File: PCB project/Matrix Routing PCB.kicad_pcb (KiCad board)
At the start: 4 copper layers, 87 x 35 mm, 14 parts, among them J1 53261-0471, J2 JST_PH_S4B-PH-SM4-TB, J3 ESQ-105-23-T-D, J4 TSM-102-01-L-DH-A, J5 USB-A-S-F-B-SM2-R-TR, U1 FT232RL

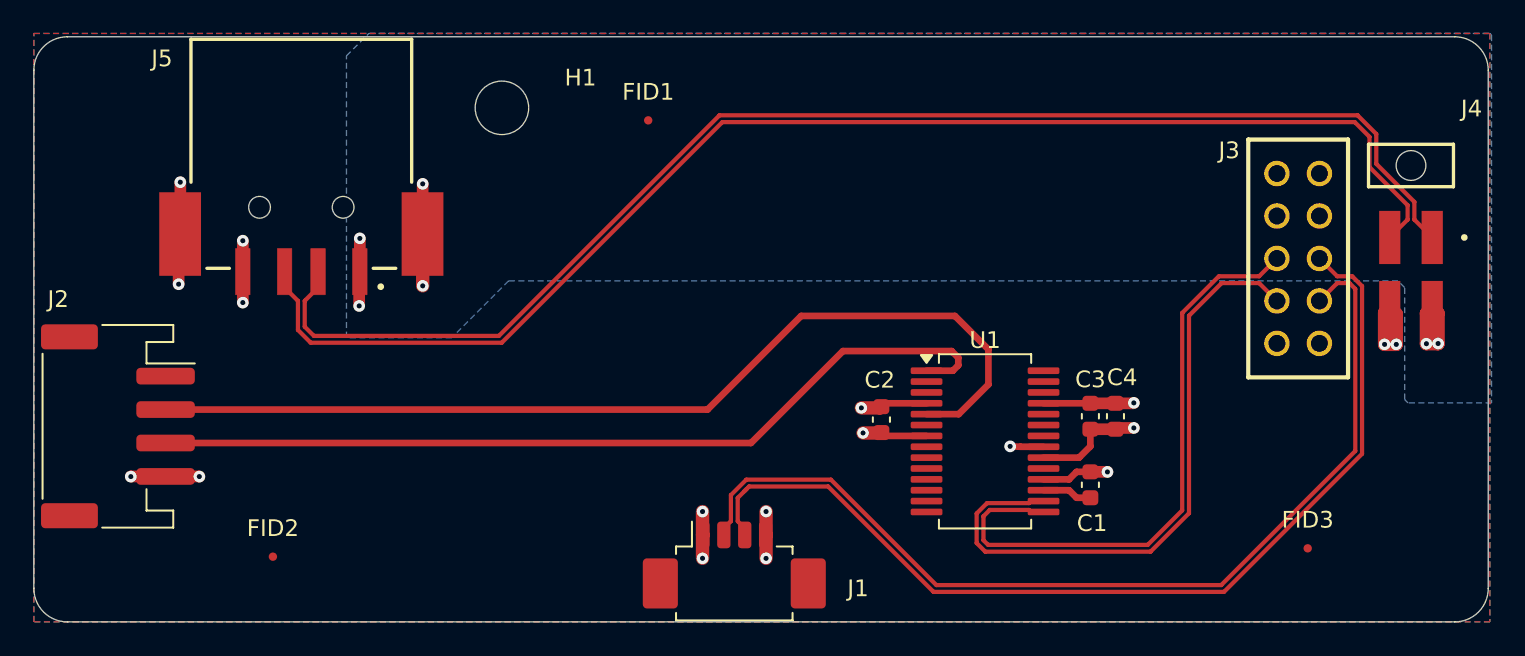
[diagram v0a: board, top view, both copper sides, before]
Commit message: Move J2 2.41mm forward
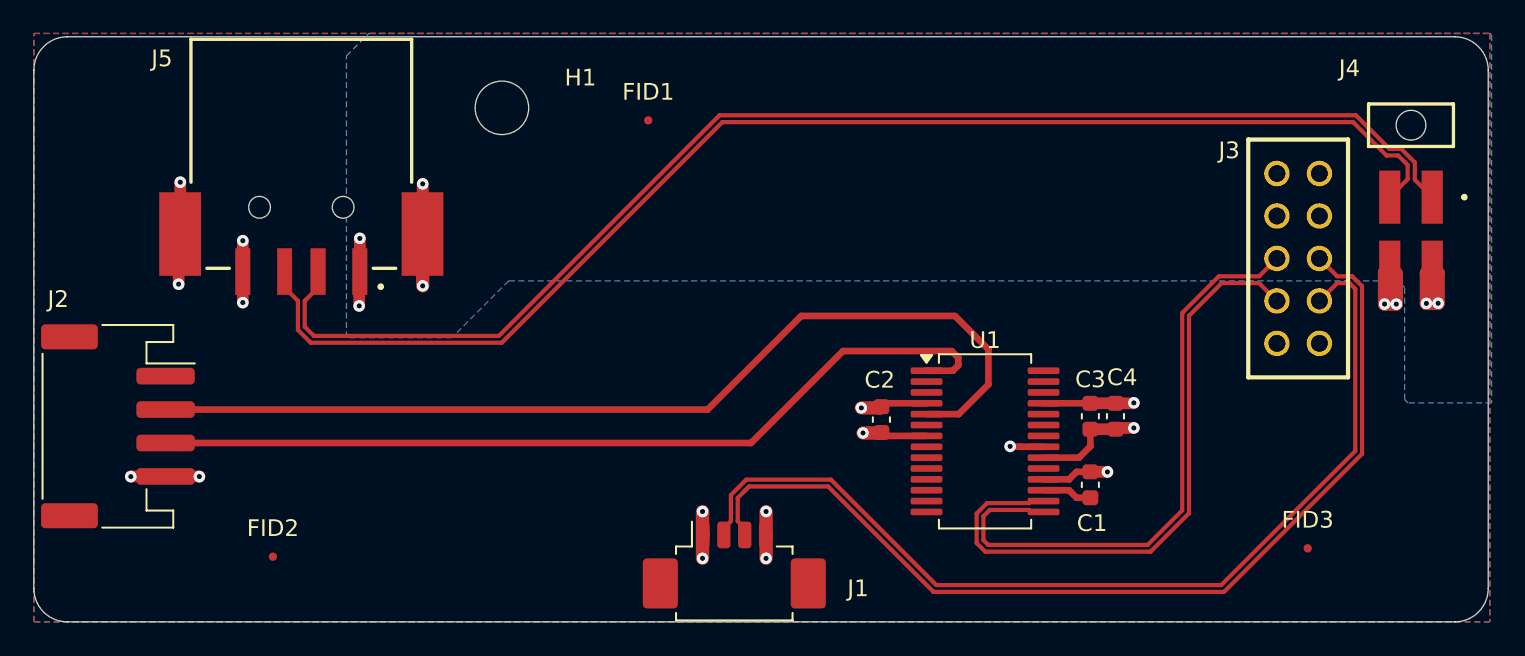
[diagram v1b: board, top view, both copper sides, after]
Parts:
- moved J4 2.41 mm to (257.3, 76.9)
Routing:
- net /USB_OTG_DN: track 81.5 -> 79.4 mm
- net /USB_OTG_DP: track 81.5 -> 79.4 mm
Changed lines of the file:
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@@
 	(footprint "Matrix Routing PCB:SAMTEC_TSM-102-01-L-DH-A"
 		(layer "F.Cu")
-		(at 257.279151 79.275)
+		(at 257.279151 76.865)
 		(property "Reference" "J4"
-			(at 3.620849 -3.4 0)
+			(at -3.679151 -3.4 0)
 			(layer "F.SilkS")
 			(effects
@@
 		(layer "Dwgs.User")
 		(pts
-			(xy 257.279151 78.005) (xy 257.279151 71.575)
-		)
-		(height 0)
-		(orientation 1)
-		(format
-			(prefix "")
-			(suffix "")
-			(units 3)
-			(units_format 0)
-			(precision 4)
-			(suppress_zeroes yes)
-		)
-		(style
-			(thickness 0.1)
-			(arrow_length 1.27)
-			(text_position_mode 0)
-			(arrow_direction outward)
-			(extension_height 0.58642)
-			(extension_offset 0.5)
-			(keep_text_aligned yes)
-		)
-		(gr_text "6.43"
-			(at 256.129151 74.79 90)
-			(layer "Dwgs.User")
-			(effects
-				(font
-					(size 1 1)
-					(thickness 0.15)
-				)
-			)
-		)
-	)
-	(dimension
-		(type orthogonal)
-		(layer "Dwgs.User")
-		(pts
 			(xy 248.054 78.231) (xy 248.054 71.575)
 		)
@@
 		(layer "Dwgs.User")
 		(pts
-			(xy 257.03 92.26) (xy 257.03 106.575)
-		)
-		(height 0)
-		(orientation 1)
-		(format
-			(prefix "")
-			(suffix "")
-			(units 3)
-			(units_format 0)
-			(precision 4)
-			(suppress_zeroes yes)
-		)
-		(style
-			(thickness 0.1)
-			(arrow_length 1.27)
-			(text_position_mode 0)
-			(arrow_direction outward)
-			(extension_height 0.58642)
-			(extension_offset 0.5)
-			(keep_text_aligned yes)
-		)
-		(gr_text "14.315"
-			(at 255.88 99.4175 90)
-			(layer "Dwgs.User")
-			(effects
-				(font
-					(size 1 1)
-					(thickness 0.15)
-				)
-			)
-		)
-	)
-	(dimension
-		(type orthogonal)
-		(layer "Dwgs.User")
-		(pts
 			(xy 174.9 106.575) (xy 261.9 106.575)
 		)
@@
 	)
 	(segment
-		(start 255.7 88.079151)
-		(end 256.009151 87.77)
+		(start 255.7 85.669151)
+		(end 256.009151 85.36)
 		(width 0.8)
 		(layer "F.Cu")
@@
 	)
 	(segment
-		(start 256.4 88.160849)
-		(end 256.009151 87.77)
+		(start 256.4 85.750849)
+		(end 256.009151 85.36)
 		(width 0.8)
 		(layer "F.Cu")
@@
 	)
 	(segment
-		(start 255.7 89.975)
-		(end 255.7 88.079151)
+		(start 255.7 87.565)
+		(end 255.7 85.669151)
 		(width 0.8)
 		(layer "F.Cu")
@@
 	)
 	(segment
-		(start 256.4 89.975)
-		(end 256.4 88.160849)
+		(start 256.4 87.565)
+		(end 256.4 85.750849)
 		(width 0.8)
 		(layer "F.Cu")
@@
 	)
 	(segment
-		(start 255.7 89.975)
-		(end 256.4 89.975)
+		(start 255.7 87.565)
+		(end 256.4 87.565)
 		(width 0.8)
 		(layer "F.Cu")
@@
 	)
 	(via
-		(at 256.4 89.975)
+		(at 256.4 87.565)
 		(size 0.7)
 		(drill 0.3)
@@
 	)
 	(via
-		(at 255.7 89.975)
+		(at 255.7 87.565)
 		(size 0.7)
 		(drill 0.3)
@@
 	)
 	(segment
-		(start 191.103 87.372)
-		(end 191.9 86.575)
+		(start 257.508 80.128849)
+		(end 257.508 79.095914)
 		(width 0.254)
 		(layer "F.Cu")
@@
 	)
 	(segment
-		(start 258.549151 83.58)
-		(end 257.482151 82.513)
+		(start 256.684086 78.272)
+		(end 255.984086 78.272)
 		(width 0.254)
 		(layer "F.Cu")
@@
 	)
 	(segment
-		(start 215.915914 76.272)
-		(end 202.718916 89.469)
+		(start 202.718916 89.469)
+		(end 191.654425 89.469)
 		(width 0.254)
 		(layer "F.Cu")
@@
 	)
 	(segment
-		(start 257.482151 82.513)
-		(end 257.482151 81.454151)
+		(start 215.915914 76.272)
+		(end 202.718916 89.469)
 		(width 0.254)
 		(layer "F.Cu")
@@
 	)
 	(segment
-		(start 255.203 77.390914)
-		(end 254.084084 76.272)
+		(start 258.549151 81.17)
+		(end 257.508 80.128849)
 		(width 0.254)
 		(layer "F.Cu")
@@
 	)
 	(segment
-		(start 191.9 86.575)
-		(end 191.9 85.625)
+		(start 257.508 79.095914)
+		(end 256.684086 78.272)
 		(width 0.254)
 		(layer "F.Cu")
@@
 	)
 	(segment
-		(start 255.203 77.390914)
-		(end 255.203 79.175)
+		(start 191.103 88.917575)
+		(end 191.103 87.372)
 		(width 0.254)
 		(layer "F.Cu")
@@
 	)
 	(segment
-		(start 191.103 88.917575)
-		(end 191.103 87.372)
+		(start 255.984086 78.272)
+		(end 253.984086 76.272)
 		(width 0.254)
 		(layer "F.Cu")
@@
 	)
 	(segment
-		(start 257.482151 81.454151)
-		(end 255.203 79.175)
+		(start 191.654425 89.469)
+		(end 191.103 88.917575)
 		(width 0.254)
 		(layer "F.Cu")
@@
 	)
 	(segment
-		(start 254.084084 76.272)
-		(end 215.915914 76.272)
+		(start 191.9 86.575)
+		(end 191.9 85.625)
 		(width 0.254)
 		(layer "F.Cu")
@@
 	)
 	(segment
-		(start 191.654425 89.469)
-		(end 202.718916 89.469)
+		(start 253.984086 76.272)
+		(end 215.915914 76.272)
 		(width 0.254)
 		(layer "F.Cu")
@@
 	)
 	(segment
-		(start 191.654425 89.469)
-		(end 191.103 88.917575)
+		(start 191.103 87.372)
+		(end 191.9 86.575)
 		(width 0.254)
 		(layer "F.Cu")
@@
 	)
 	(segment
-		(start 258.2 88.119151)
-		(end 258.549151 87.77)
+		(start 258.2 85.709151)
+		(end 258.549151 85.36)
 		(width 0.8)
 		(layer "F.Cu")
@@
 	)
 	(segment
-		(start 258.2 89.935)
-		(end 258.2 88.119151)
+		(start 258.2 87.525)
+		(end 258.2 85.709151)
 		(width 0.8)
 		(layer "F.Cu")
@@
 	)
 	(segment
-		(start 258.9 89.925)
-		(end 258.9 88.120849)
+		(start 258.9 87.515)
+		(end 258.9 85.710849)
 		(width 0.8)
 		(layer "F.Cu")
@@
 	)
 	(segment
-		(start 258.89 89.935)
-		(end 258.9 89.925)
+		(start 258.89 87.525)
+		(end 258.9 87.515)
 		(width 0.8)
 		(layer "F.Cu")
@@
 	)
 	(segment
-		(start 258.2 89.935)
-		(end 258.89 89.935)
+		(start 258.2 87.525)
+		(end 258.89 87.525)
 		(width 0.8)
 		(layer "F.Cu")
@@
 	)
 	(segment
-		(start 258.9 88.120849)
-		(end 258.549151 87.77)
+		(start 258.9 85.710849)
+		(end 258.549151 85.36)
 		(width 0.8)
 		(layer "F.Cu")
@@
 	)
 	(via
-		(at 258.2 89.935)
+		(at 258.2 87.525)
 		(size 0.7)
 		(drill 0.3)
@@
 	)
 	(via
-		(at 258.9 89.925)
+		(at 258.9 87.515)
 		(size 0.7)
 		(drill 0.3)
@@
 	)
 	(segment
-		(start 216.084914 76.68)
-		(end 253.915085 76.68)
+		(start 190.697 87.372)
+		(end 189.9 86.575)
 		(width 0.254)
 		(layer "F.Cu")
@@
 	)
 	(segment
-		(start 253.915085 76.68)
-		(end 254.795 77.559913)
+		(start 257.076151 79.238237)
+		(end 256.515914 78.678)
 		(width 0.254)
 		(layer "F.Cu")
@@
 	)
 	(segment
-		(start 190.697 89.111575)
-		(end 191.462425 89.877)
+		(start 191.462425 89.877)
+		(end 190.697 89.111575)
 		(width 0.254)
 		(layer "F.Cu")
@@
 	)
 	(segment
-		(start 189.9 85.625)
-		(end 189.9 86.575)
+		(start 255.815914 78.678)
+		(end 253.817914 76.68)
 		(width 0.254)
 		(layer "F.Cu")
@@
 	)
 	(segment
-		(start 254.795 77.559913)
-		(end 254.795 79.37)
+		(start 256.515914 78.678)
+		(end 255.815914 78.678)
 		(width 0.254)
 		(layer "F.Cu")
@@
 	)
 	(segment
-		(start 189.9 86.575)
-		(end 190.697 87.372)
+		(start 202.887915 89.877)
+		(end 191.462425 89.877)
 		(width 0.254)
 		(layer "F.Cu")
@@
 	)
 	(segment
-		(start 257.076151 82.513)
-		(end 256.009151 83.58)
+		(start 257.076151 80.103)
+		(end 257.076151 79.238237)
 		(width 0.254)
 		(layer "F.Cu")
@@
 	)
 	(segment
-		(start 191.462425 89.877)
-		(end 202.887915 89.877)
+		(start 189.9 86.575)
+		(end 189.9 85.625)
 		(width 0.254)
 		(layer "F.Cu")
@@
 	)
 	(segment
-		(start 202.887915 89.877)
+		(start 253.817914 76.68)
 		(end 216.084914 76.68)
 		(width 0.254)
@@
 	)
 	(segment
-		(start 257.076151 81.651151)
-		(end 257.076151 82.513)
+		(start 256.009151 81.17)
+		(end 257.076151 80.103)
 		(width 0.254)
 		(layer "F.Cu")
@@
 	)
 	(segment
-		(start 254.795 79.37)
-		(end 257.076151 81.651151)
+		(start 216.084914 76.68)
+		(end 202.887915 89.877)
 		(width 0.254)
 		(layer "F.Cu")
@@
 	)
 	(segment
-		(start 190.697 87.372)
-		(end 190.697 89.111575)
+		(start 190.697 89.111575)
+		(end 190.697 87.372)
 		(width 0.254)
 		(layer "F.Cu")

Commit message: Move J2 1.27mm back
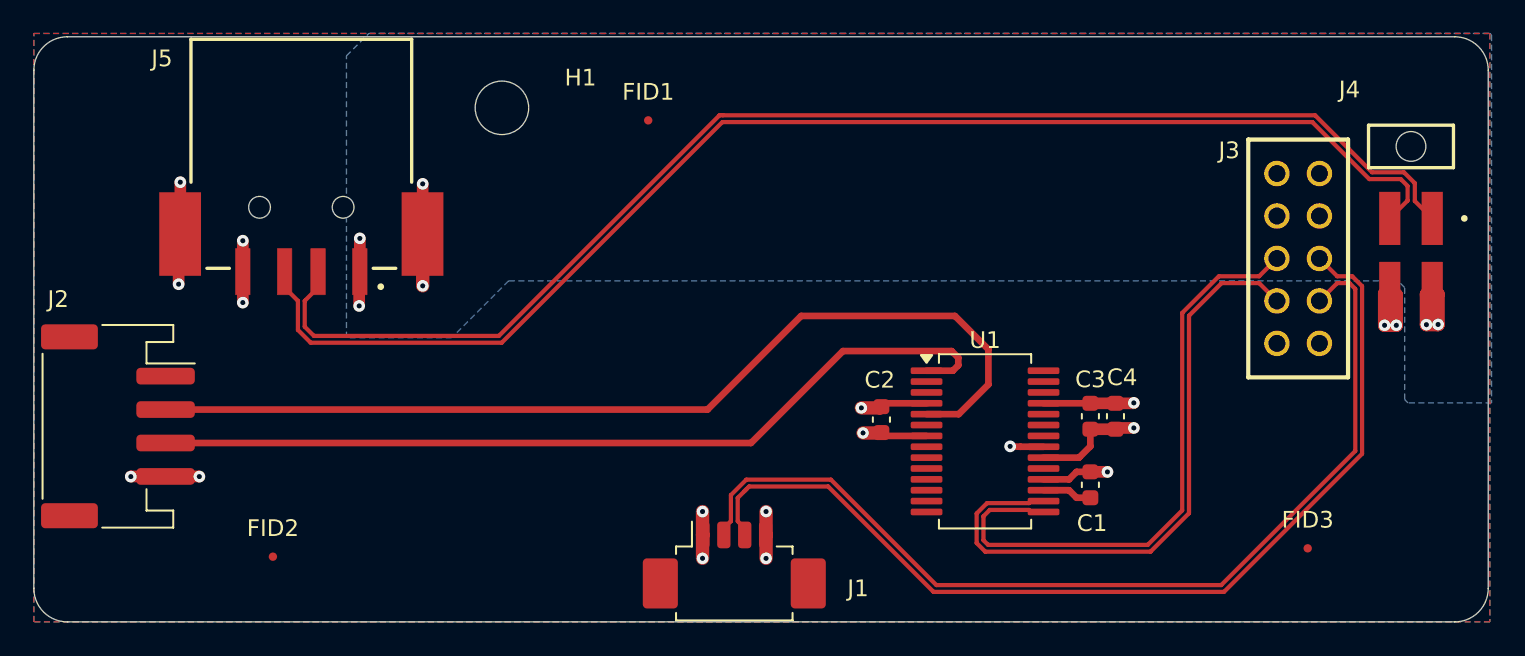
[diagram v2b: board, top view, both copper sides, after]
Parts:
- moved J4 1.27 mm to (257.3, 78.1)
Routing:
- net /USB_OTG_DN: track 79.4 -> 79.9 mm
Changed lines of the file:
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@@
 	(footprint "Matrix Routing PCB:SAMTEC_TSM-102-01-L-DH-A"
 		(layer "F.Cu")
-		(at 257.279151 76.865)
+		(at 257.279151 78.135)
 		(property "Reference" "J4"
 			(at -3.679151 -3.4 0)
@@
 	)
 	(segment
-		(start 255.7 85.669151)
-		(end 256.009151 85.36)
+		(start 255.7 86.939151)
+		(end 256.009151 86.63)
 		(width 0.8)
 		(layer "F.Cu")
@@
 	)
 	(segment
-		(start 256.4 85.750849)
-		(end 256.009151 85.36)
+		(start 256.4 87.020849)
+		(end 256.009151 86.63)
 		(width 0.8)
 		(layer "F.Cu")
@@
 	)
 	(segment
-		(start 255.7 87.565)
-		(end 255.7 85.669151)
+		(start 255.7 88.835)
+		(end 255.7 86.939151)
 		(width 0.8)
 		(layer "F.Cu")
@@
 	)
 	(segment
-		(start 256.4 87.565)
-		(end 256.4 85.750849)
+		(start 256.4 88.835)
+		(end 256.4 87.020849)
 		(width 0.8)
 		(layer "F.Cu")
@@
 	)
 	(segment
-		(start 255.7 87.565)
-		(end 256.4 87.565)
+		(start 255.7 88.835)
+		(end 256.4 88.835)
 		(width 0.8)
 		(layer "F.Cu")
@@
 	)
 	(via
-		(at 256.4 87.565)
+		(at 256.4 88.835)
 		(size 0.7)
 		(drill 0.3)
@@
 	)
 	(via
-		(at 255.7 87.565)
+		(at 255.7 88.835)
 		(size 0.7)
 		(drill 0.3)
@@
 	)
 	(segment
-		(start 257.508 80.128849)
-		(end 257.508 79.095914)
+		(start 191.103 87.372)
+		(end 191.9 86.575)
 		(width 0.254)
 		(layer "F.Cu")
@@
 	)
 	(segment
-		(start 256.684086 78.272)
-		(end 255.984086 78.272)
+		(start 258.549151 82.44)
+		(end 257.508 81.398849)
 		(width 0.254)
 		(layer "F.Cu")
@@
 	)
 	(segment
-		(start 202.718916 89.469)
-		(end 191.654425 89.469)
+		(start 191.654425 89.469)
+		(end 191.103 88.917575)
+		(width 0.254)
+		(layer "F.Cu")
+		(net "/USB_OTG_DN")
+	)
+	(segment
+		(start 191.9 86.575)
+		(end 191.9 85.625)
 		(width 0.254)
 		(layer "F.Cu")
@@
 	)
 	(segment
-		(start 215.915914 76.272)
+		(start 215.915916 76.272)
 		(end 202.718916 89.469)
 		(width 0.254)
@@
 	)
 	(segment
-		(start 258.549151 81.17)
-		(end 257.508 80.128849)
+		(start 257.508 80.333)
+		(end 256.857 79.682)
 		(width 0.254)
 		(layer "F.Cu")
@@
 	)
 	(segment
-		(start 257.508 79.095914)
-		(end 256.684086 78.272)
+		(start 202.718916 89.469)
+		(end 191.654425 89.469)
 		(width 0.254)
 		(layer "F.Cu")
@@
 	)
 	(segment
-		(start 191.103 88.917575)
-		(end 191.103 87.372)
+		(start 254.954086 79.682)
+		(end 251.544086 76.272)
 		(width 0.254)
 		(layer "F.Cu")
@@
 	)
 	(segment
-		(start 255.984086 78.272)
-		(end 253.984086 76.272)
+		(start 256.857 79.682)
+		(end 254.954086 79.682)
 		(width 0.254)
 		(layer "F.Cu")
@@
 	)
 	(segment
-		(start 191.654425 89.469)
-		(end 191.103 88.917575)
+		(start 191.103 88.917575)
+		(end 191.103 87.372)
 		(width 0.254)
 		(layer "F.Cu")
@@
 	)
 	(segment
-		(start 191.9 86.575)
-		(end 191.9 85.625)
+		(start 251.544086 76.272)
+		(end 216.12 76.272)
 		(width 0.254)
 		(layer "F.Cu")
@@
 	)
 	(segment
-		(start 253.984086 76.272)
-		(end 215.915914 76.272)
+		(start 257.508 81.398849)
+		(end 257.508 80.333)
 		(width 0.254)
 		(layer "F.Cu")
@@
 	)
 	(segment
-		(start 191.103 87.372)
-		(end 191.9 86.575)
+		(start 216.12 76.272)
+		(end 215.915916 76.272)
 		(width 0.254)
 		(layer "F.Cu")
@@
 	)
 	(segment
-		(start 258.2 85.709151)
-		(end 258.549151 85.36)
+		(start 258.2 86.979151)
+		(end 258.549151 86.63)
 		(width 0.8)
 		(layer "F.Cu")
@@
 	)
 	(segment
-		(start 258.2 87.525)
-		(end 258.2 85.709151)
+		(start 258.2 88.795)
+		(end 258.2 86.979151)
 		(width 0.8)
 		(layer "F.Cu")
@@
 	)
 	(segment
-		(start 258.9 87.515)
-		(end 258.9 85.710849)
+		(start 258.9 88.785)
+		(end 258.9 86.980849)
 		(width 0.8)
 		(layer "F.Cu")
@@
 	)
 	(segment
-		(start 258.89 87.525)
-		(end 258.9 87.515)
+		(start 258.89 88.795)
+		(end 258.9 88.785)
 		(width 0.8)
 		(layer "F.Cu")
@@
 	)
 	(segment
-		(start 258.2 87.525)
-		(end 258.89 87.525)
+		(start 258.2 88.795)
+		(end 258.89 88.795)
 		(width 0.8)
 		(layer "F.Cu")
@@
 	)
 	(segment
-		(start 258.9 85.710849)
-		(end 258.549151 85.36)
+		(start 258.9 86.980849)
+		(end 258.549151 86.63)
 		(width 0.8)
 		(layer "F.Cu")
@@
 	)
 	(via
-		(at 258.2 87.525)
+		(at 258.2 88.795)
 		(size 0.7)
 		(drill 0.3)
@@
 	)
 	(via
-		(at 258.9 87.515)
+		(at 258.9 88.785)
 		(size 0.7)
 		(drill 0.3)
@@
 	)
 	(segment
-		(start 190.697 87.372)
-		(end 189.9 86.575)
+		(start 254.785914 80.088)
+		(end 251.375914 76.678)
 		(width 0.254)
 		(layer "F.Cu")
@@
 	)
 	(segment
-		(start 257.076151 79.238237)
-		(end 256.515914 78.678)
+		(start 191.462425 89.877)
+		(end 190.697 89.111575)
 		(width 0.254)
 		(layer "F.Cu")
@@
 	)
 	(segment
-		(start 191.462425 89.877)
-		(end 190.697 89.111575)
+		(start 216.084914 76.68)
+		(end 202.887915 89.877)
 		(width 0.254)
 		(layer "F.Cu")
@@
 	)
 	(segment
-		(start 255.815914 78.678)
-		(end 253.817914 76.68)
+		(start 256.665914 80.088)
+		(end 254.785914 80.088)
 		(width 0.254)
 		(layer "F.Cu")
@@
 	)
 	(segment
-		(start 256.515914 78.678)
-		(end 255.815914 78.678)
+		(start 190.697 87.372)
+		(end 189.9 86.575)
 		(width 0.254)
 		(layer "F.Cu")
@@
 	)
 	(segment
-		(start 202.887915 89.877)
-		(end 191.462425 89.877)
+		(start 251.375914 76.678)
+		(end 216.12 76.678)
 		(width 0.254)
 		(layer "F.Cu")
@@
 	)
 	(segment
-		(start 257.076151 80.103)
-		(end 257.076151 79.238237)
+		(start 257.066457 80.488543)
+		(end 256.665914 80.088)
 		(width 0.254)
 		(layer "F.Cu")
@@
 	)
 	(segment
-		(start 189.9 86.575)
-		(end 189.9 85.625)
+		(start 202.887915 89.877)
+		(end 191.462425 89.877)
 		(width 0.254)
 		(layer "F.Cu")
@@
 	)
 	(segment
-		(start 253.817914 76.68)
-		(end 216.084914 76.68)
+		(start 257.076151 81.373)
+		(end 257.076151 80.508237)
 		(width 0.254)
 		(layer "F.Cu")
@@
 	)
 	(segment
-		(start 256.009151 81.17)
-		(end 257.076151 80.103)
+		(start 190.697 89.111575)
+		(end 190.697 87.372)
 		(width 0.254)
 		(layer "F.Cu")
@@
 	)
 	(segment
-		(start 216.084914 76.68)
-		(end 202.887915 89.877)
+		(start 256.009151 82.44)
+		(end 257.076151 81.373)
 		(width 0.254)
 		(layer "F.Cu")
@@
 	)
 	(segment
-		(start 190.697 89.111575)
-		(end 190.697 87.372)
+		(start 189.9 86.575)
+		(end 189.9 85.625)
 		(width 0.254)
 		(layer "F.Cu")

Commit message: Add stitching vias
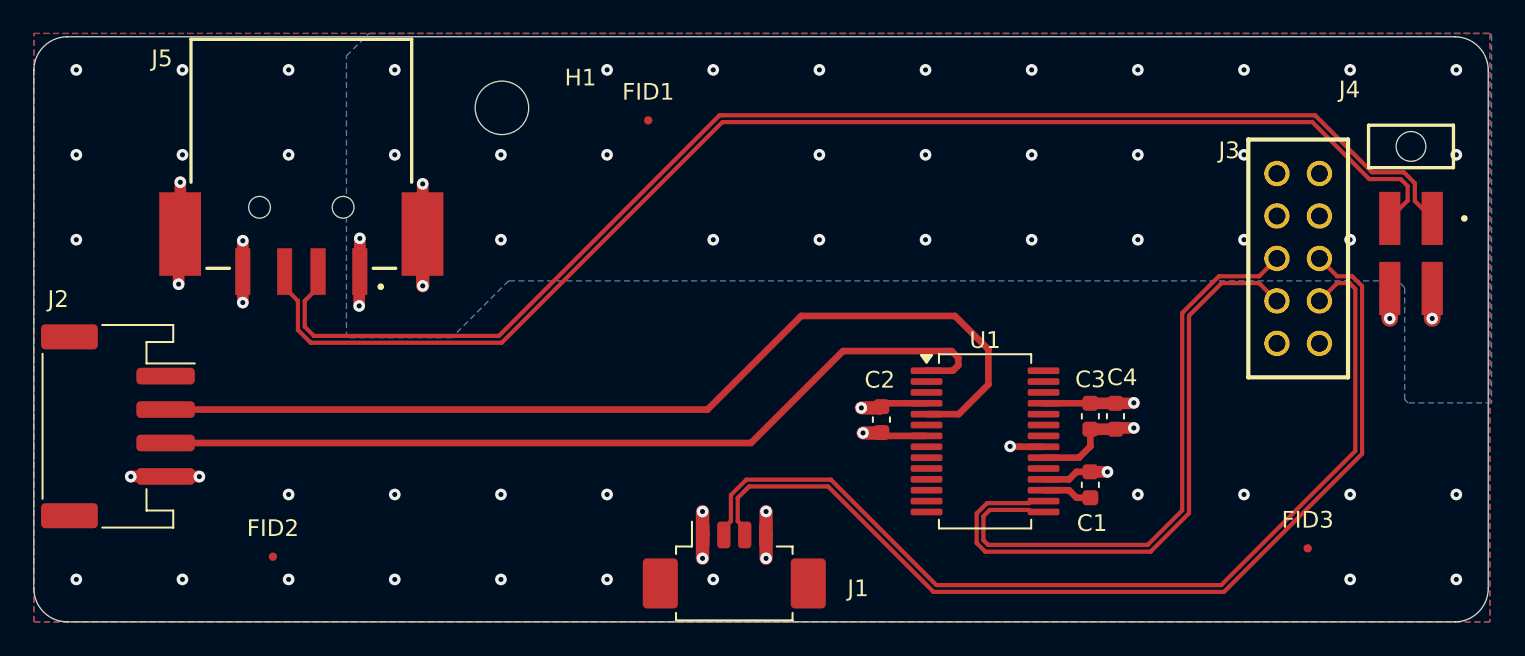
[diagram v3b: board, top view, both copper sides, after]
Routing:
- net GND: track 44.1 -> 40.5 mm, vias 16 -> 66
- net VBUS: track 9.63 -> 6.11 mm, vias 4 -> 3
